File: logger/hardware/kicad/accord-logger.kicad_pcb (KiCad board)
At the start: 2 copper layers, 120 x 80 mm, 31 parts, among them J1 Board connector 14-way, J5 SD breakout 6-way, Q5 IPD50P04P4L-11, Q6 2N3904, Q7 2N3904, U1 RaspberryPi_Pico_W, U6 LM2678T-5.0

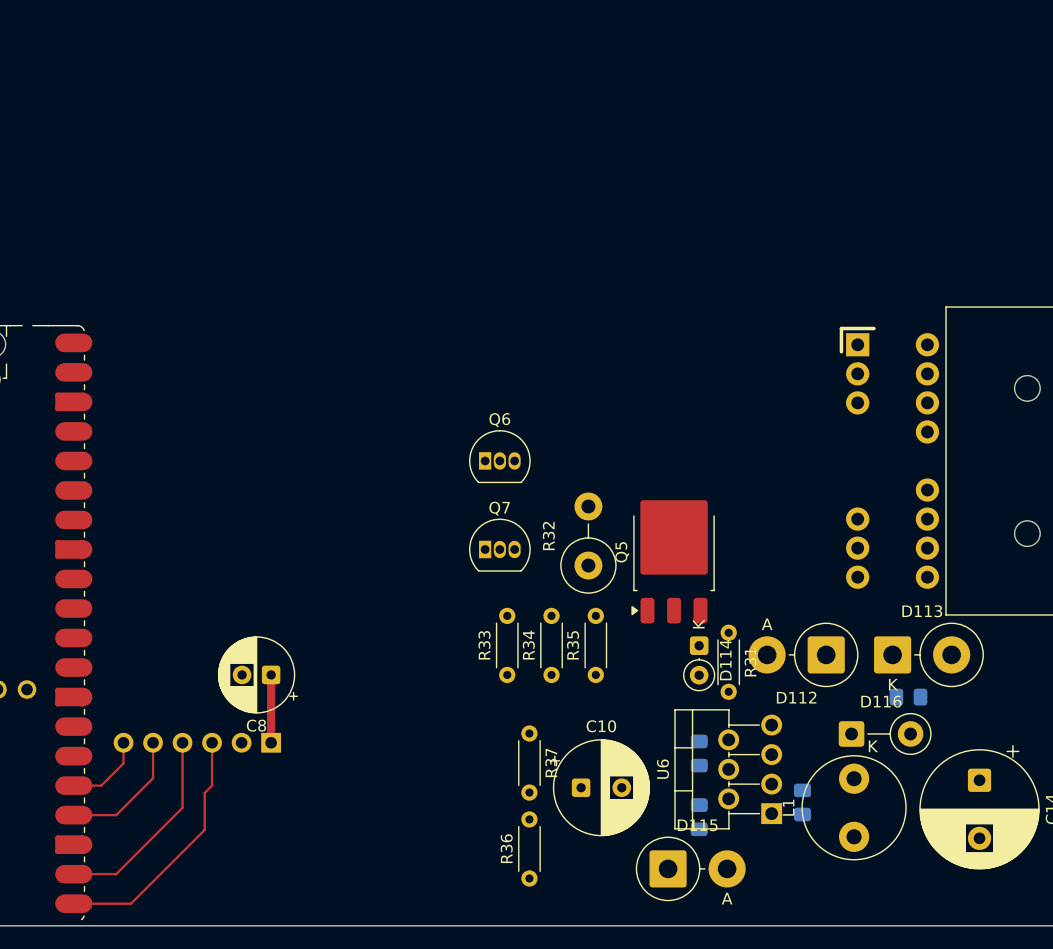
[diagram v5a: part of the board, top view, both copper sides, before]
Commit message: layout: rtc step placed; power block traces
Owner switched on the rtc step (six on_board flags) and placed U16, C25,
R50-R52 and BT1 (back) at the USB end; routed the power block.
Scratch DRC: schematic parity 0, no clearance or courtyard errors.

Open from review:
- P12 not joined between D112 cathode and Q5 pin 3 (B.Cu/F.Cu islands).
- VIN_SW reaches Q5's middle-lead pad, not the tab; a standard DPAK's
  middle lead is cut short, so route to the tab.
- PGND (35 connections) unrouted: buck return C10-, U6.4, D115 A, C14-
  still open; no pour yet.
- Unrouted: R51 pin 1 (3V3), R37 pin 1 (B5), Q7.2-R35 (HOLD_B),
  U1.33-J1.10 (AGND, comes with the inputs).
Routed buck paths: C11-U6.2 2.0 mm, C12 2.6/2.1, C13 2.4, U6.1-D115 10.5,
U6.1-L1 7.9, C10+-U6.2 14.7, L1-C14+ 13.0. I2C runs ~60 mm, at least
45 mm from the SW node.

Claude-Session-ID: 42dd0e33-28b5-4936-847e-9c2e1d2488fa
Co-Authored-By: Claude Opus 5.5 <noreply@anthropic.com>
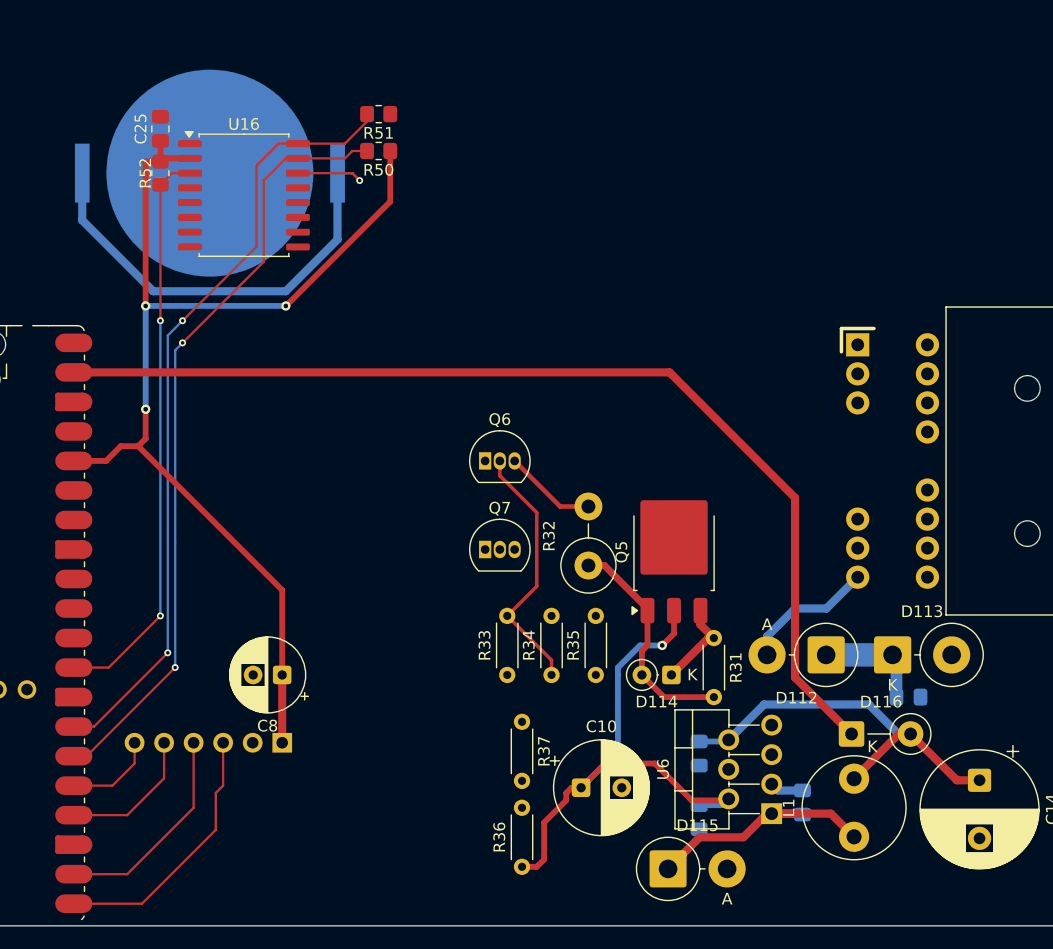
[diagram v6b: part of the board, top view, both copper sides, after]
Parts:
- added BT1: BR2032, Battery:BatteryHolder_Keystone_3034_1x20mm, B.Cu at (130.0, 74.9)
- added C25: 100nF, Capacitor_SMD:C_0805_2012Metric_Pad1.18x1.45mm_HandSolder, F.Cu at (125.7, 71.1)
- added R50: 4.7k, Resistor_SMD:R_0805_2012Metric_Pad1.20x1.40mm_HandSolder, F.Cu at (144.5, 73.0)
- added R51: 4.7k, Resistor_SMD:R_0805_2012Metric_Pad1.20x1.40mm_HandSolder, F.Cu at (144.5, 69.8)
- added R52: 10k, Resistor_SMD:R_0805_2012Metric_Pad1.20x1.40mm_HandSolder, F.Cu at (125.7, 74.9)
- added U16: DS3231SN, Package_SO:SOIC-16W_7.5x10.3mm_P1.27mm, F.Cu at (132.9, 76.8)
- moved D114 3.47 mm to (169.7, 118.1), turned to 180 degrees
- moved R31 1.35 mm to (173.4, 114.9)
- moved R37 1.19 mm to (156.8, 122.1)
- moved R36 1.19 mm to (156.8, 134.6)
- moved C8 0.95 mm to (136.2, 118.1)
- moved J5 0.95 mm to (136.2, 123.9)
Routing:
- net /P3V3_SW: track 5.83 -> 96.3 mm, vias 0 -> 3
- net /VSYS: track 0.00 -> 88.9 mm
- net /RTC_SCL: track 0.00 -> 67.5 mm, vias 0 -> 2
- net /RTC_SDA: track 0.00 -> 66.9 mm, vias 0 -> 2
- net /RTC_INT: track 0.00 -> 49.4 mm, vias 0 -> 2
- net /VIN_SW: track 0.00 -> 47.5 mm, vias 0 -> 1
- net /RTC_VBAT: track 0.00 -> 43.9 mm, vias 0 -> 1
- net /B5: track 0.00 -> 34.6 mm
- net /IGN_B: track 0.00 -> 22.4 mm
- net /SW: track 0.00 -> 21.5 mm
- net /GATE: track 0.00 -> 19.5 mm
- net /P12: track 0.00 -> 17.3 mm
- net /BATT_IN: track 0.00 -> 11.5 mm
- net /SINK: track 0.00 -> 7.97 mm
- net /BOOST: track 0.00 -> 2.87 mm
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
